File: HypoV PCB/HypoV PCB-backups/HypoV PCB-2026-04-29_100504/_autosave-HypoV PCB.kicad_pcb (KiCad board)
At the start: 2 copper layers, 61.5 x 43 mm, 12 parts, among them J1 Conn_Header_JST_PH_1x02_P2mm_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

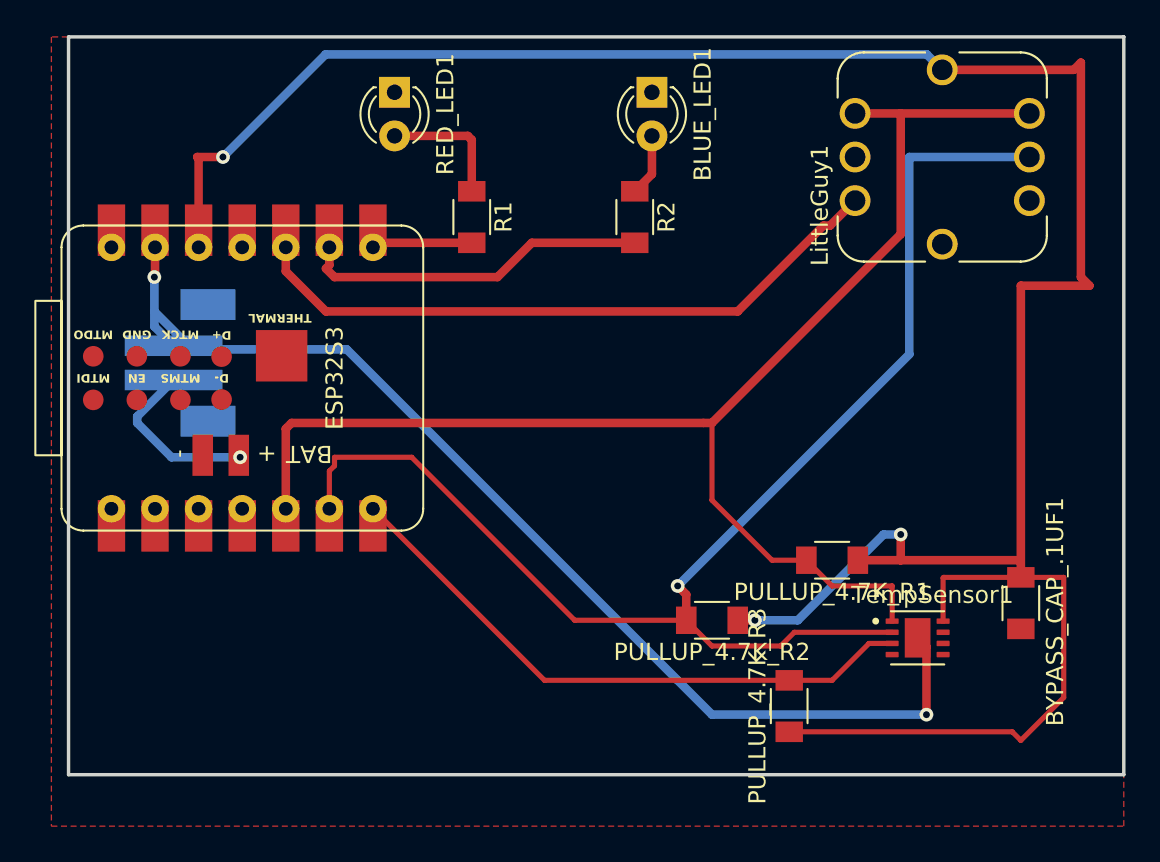
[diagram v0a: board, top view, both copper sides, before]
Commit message: added the breakout board
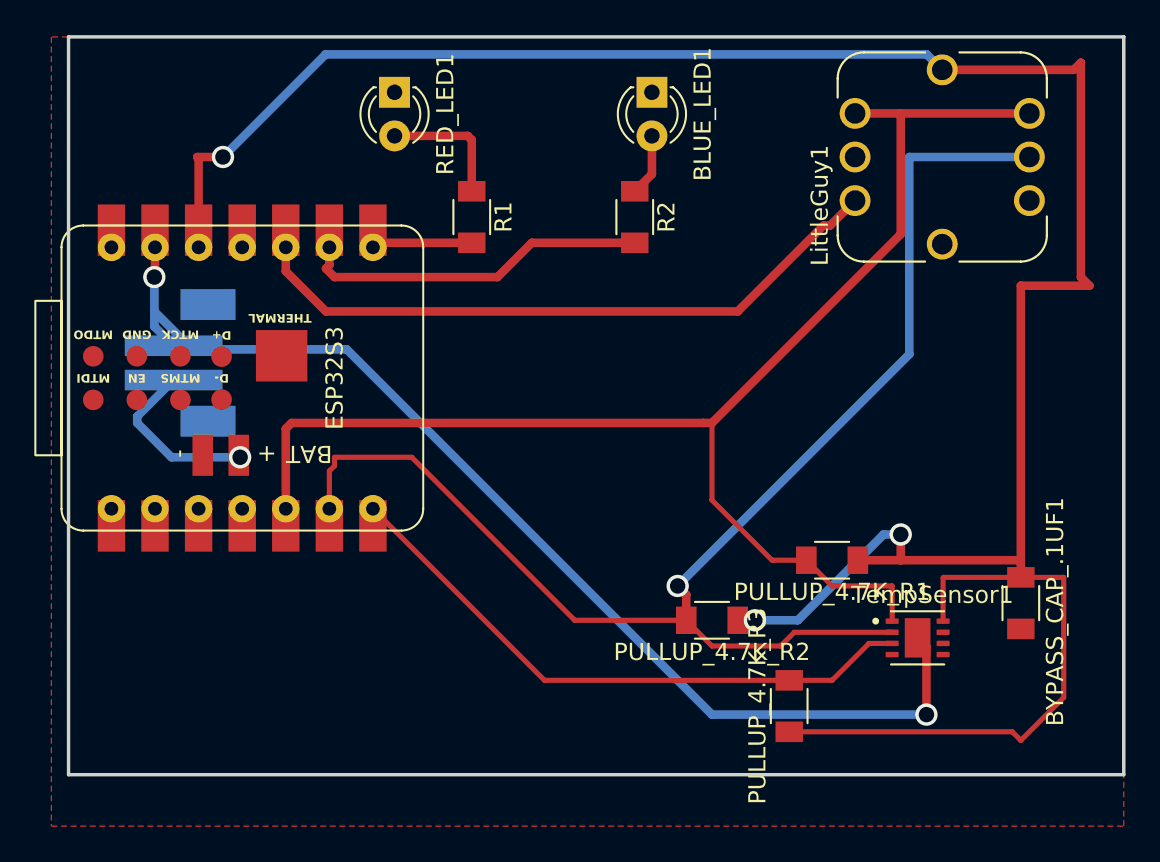
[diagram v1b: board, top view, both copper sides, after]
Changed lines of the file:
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@@
 			(outputformat 1)
 			(mirror no)
-			(drillshape 1)
+			(drillshape 0)
 			(scaleselection 1)
 			(outputdirectory "")
@@
 	(via
 		(at 76 84)
-		(size 0.8)
-		(drill 0.4)
+		(size 1.3)
+		(drill 0.9)
 		(layers "F.Cu" "B.Cu")
 		(net 1)
@@
 	(via
 		(at 121 109.5)
-		(size 0.8)
-		(drill 0.4)
+		(size 1.3)
+		(drill 0.9)
 		(layers "F.Cu" "B.Cu")
 		(net 1)
@@
 	(via
 		(at 106.5 102)
-		(size 0.8)
-		(drill 0.4)
+		(size 1.3)
+		(drill 0.9)
 		(layers "F.Cu" "B.Cu")
 		(net 2)
@@
 	(via
 		(at 80 77)
-		(size 0.8)
-		(drill 0.4)
+		(size 1.3)
+		(drill 0.9)
 		(layers "F.Cu" "B.Cu")
 		(net 4)
@@
 	(via
 		(at 111 104)
-		(size 0.8)
-		(drill 0.4)
+		(size 1.3)
+		(drill 0.9)
 		(layers "F.Cu" "B.Cu")
 		(net 4)
@@
 	(via
 		(at 119.5 99)
-		(size 0.8)
-		(drill 0.4)
+		(size 1.3)
+		(drill 0.9)
 		(layers "F.Cu" "B.Cu")
 		(net 4)
@@
 	(via
 		(at 81 94.5)
-		(size 0.8)
-		(drill 0.4)
+		(size 1.3)
+		(drill 0.9)
 		(layers "F.Cu" "B.Cu")
 		(net 14)
